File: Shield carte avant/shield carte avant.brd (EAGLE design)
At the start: 68.6 x 53.3 mm, 23 parts, among them IC1 MCP2562-E_P, IC2 MCP2515-I_P, J1 22-05-7078-07, J2 22-05-7028-02, J3 22-05-7038-03, J5 22-05-7028-02, M1 ARDUINO_R3_ICSP

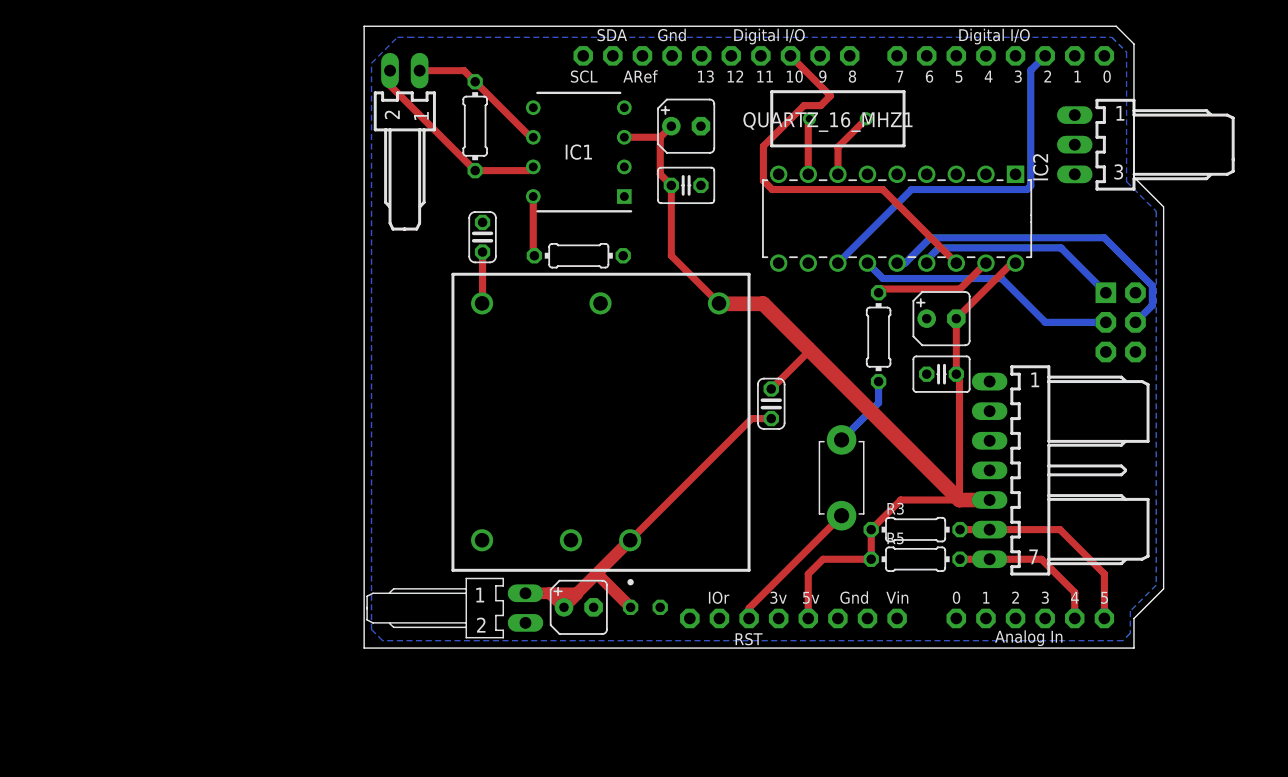
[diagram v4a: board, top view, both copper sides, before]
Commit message: Début ajout relais pour les boutons lumineux
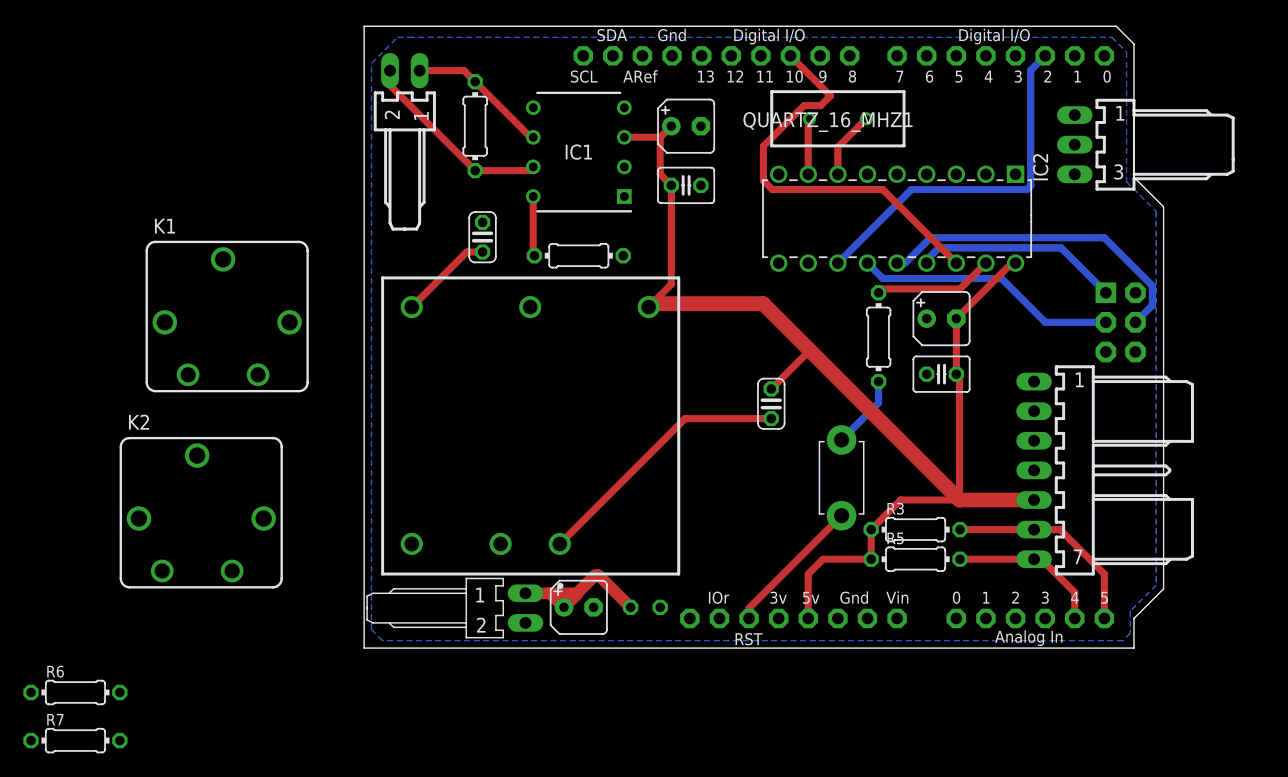
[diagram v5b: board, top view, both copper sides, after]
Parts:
- added K1, K2: CP1-12V, relay:CP1
- added R6, R7: 100R, rcl:0204/7
- moved PS1 6.04 mm to (2.86, 31.8)
- moved J1 3.81 mm to (58.7, 15.2)
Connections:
- new net S$1: C4.2, PS1.1
- net +12V: now also K1.1, K1.C, K2.1, K2.C; no longer C4.2, PS1.1
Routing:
- net S$1: track 0.00 -> 22.6 mm
- net +12V: track 34.9 -> 14.2 mm
- net +5V: track 99.4 -> 108.7 mm
- net N$3: track 4.42 -> 8.03 mm

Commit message: Ajout des MOSFET pour gérer l'affichage des boutons
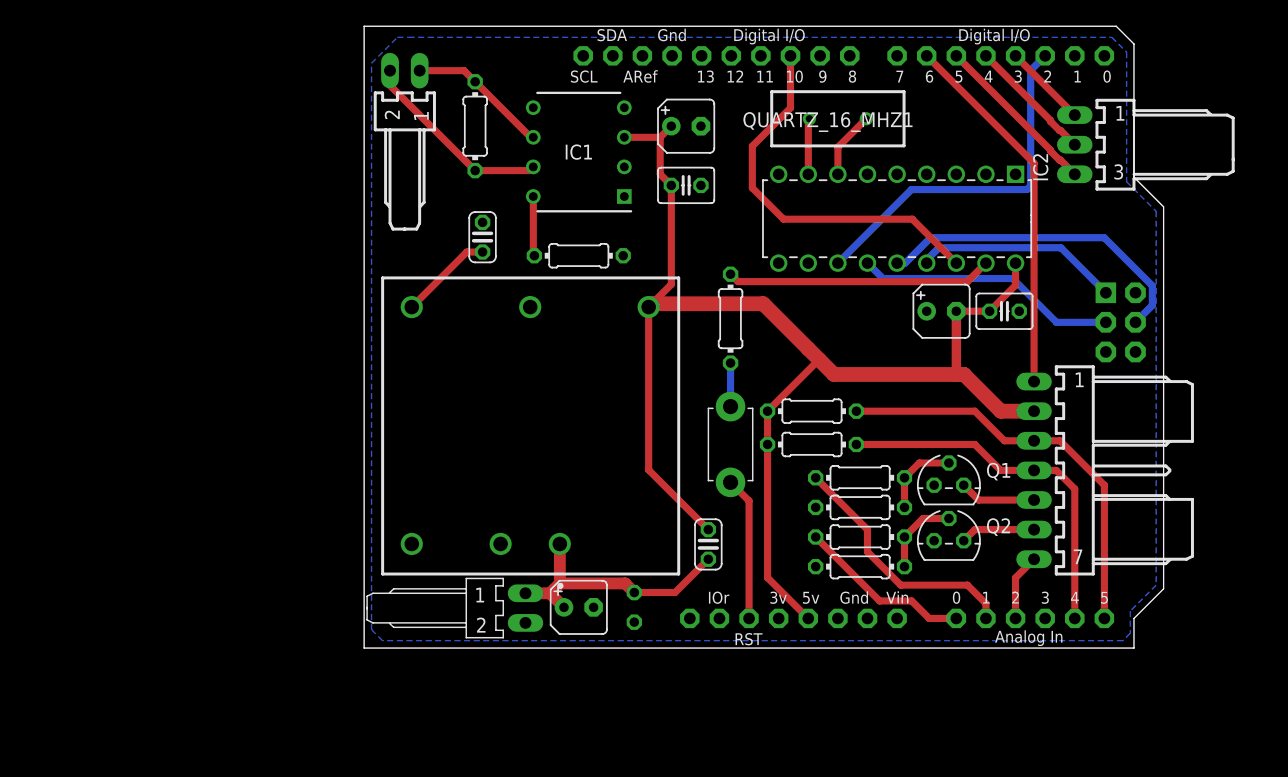
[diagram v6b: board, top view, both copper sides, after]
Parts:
- removed C4: 680 pF, rcl:C025-024X044
- removed K1, K2: CP1-12V, relay:CP1
- added C1: 680 pF, rcl:C025-024X044
- added Q1, Q2: (no value), transistors:TO-92
- added R8, R9: 100, rcl:0204/7
- R6, R7: value 100R -> 10k
- moved R7 70.2 mm to (43.8, 12.1)
- moved R6 68.2 mm to (43.8, 6.99)
- moved R3 13.5 mm to (39.7, 20.3)
- moved R5 13.3 mm to (39.7, 17.5)
- moved R4 12.8 mm to (32.7, 28.3)
- moved SW2 9.94 mm to (32.7, 17.5)
- moved C8 7.63 mm to (56.2, 28.9), turned to 180 degrees
- moved C3 0.95 mm to (24.4, 3.49), turned to 270 degrees
- moved C2 0.63 mm to (50.8, 28.9)
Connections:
- removed net D1: J3.1
- removed net D2: J3.2
- removed net D3: J3.3
- removed net D4: J1.1
- removed net D5: J1.2
- removed net D6: J1.3
- removed net D7: J1.4
- removed net S$1: C4.2, PS1.1
- removed net SCL: J1.6, M1.A5, R3.2
- removed net SDA: J1.7, M1.A4, R5.2
- new net ERROR: J1.6, Q2.3
- new net ERROR_MOTOR: M1.A0, R8.2
- new net HOMMING: M1.D12
- new net LAUNCH: J1.5, Q1.3
- new net LAUNCH_LED: M1.A1, R9.2
- new net LAUNCH_STATE: J1.7, M1.A2
- new net N$12: Q2.2, R6.2, R8.1
- new net N$13: Q1.2, R7.2, R9.1
- new net NEUTRE: J1.1, M1.D6
- new net SCL_I2C: J1.3, M1.A5, R3.2
- new net SCL_SPI: J3.3, M1.D5
- new net SDA_I2C: J1.4, M1.A4, R5.2
- new net SDA_SPI: J3.2, M1.D4
- new net TV: J3.1, M1.D3
- net +12V: now also C1.1, PS1.1; no longer K1.1, K1.C, K2.1, K2.C
- net +5V: now also C1.2, J1.2; no longer C4.1, J1.5
- net GND: now also Q1.1, Q2.1, R6.1, R7.1
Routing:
- net SCL_I2C: track 0.00 -> 35.3 mm
- net NEUTRE: track 0.00 -> 31.8 mm
- net SDA_I2C: track 0.00 -> 31.4 mm
- net S$1: track 22.6 -> 0.00 mm
- net LAUNCH_LED: track 0.00 -> 21.5 mm
- net SCL: track 17.8 -> 0.00 mm
- net ERROR_MOTOR: track 0.00 -> 15.0 mm
- net SCL_SPI: track 0.00 -> 14.4 mm
- net SDA: track 13.2 -> 0.00 mm
- net N$11: track 10.3 -> 22.8 mm
- net SDA_SPI: track 0.00 -> 10.8 mm
- net +5V: track 108.7 -> 117.5 mm
- net +12V: track 14.2 -> 22.6 mm
- net TV: track 0.00 -> 7.18 mm
- net N$12: track 0.00 -> 7.01 mm
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
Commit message: Fin du routage et vérification sérigraphie
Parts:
- moved J2 12.4 mm to (5.08, 37.1), turned to 180 degrees
- moved R2 1.59 mm to (10.8, 43.2)
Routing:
- net N$8: track 12.1 -> 20.3 mm
- net N$5: track 16.7 -> 11.1 mm
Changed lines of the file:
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@@
 <element name="C5" library="rcl" library_urn="urn:adsk.eagle:library:334" package="C025-024X044" package3d_urn="urn:adsk.eagle:package:23630/1" value="680 pF" x="11.43" y="35.2425" smashed="yes" rot="R90">
 <attribute name="SPICEPREFIX" value="C" x="11.43" y="35.2425" size="1.778" layer="27" rot="R90" display="off"/>
-<attribute name="VALUE" x="9.3345" y="33.147" size="1.27" layer="27" ratio="10" rot="R90"/>
-</element>
-<element name="J2" library="con-molex" library_urn="urn:adsk.eagle:library:165" package="7395-02" value="22-05-7028-02" x="4.7625" y="49.53" smashed="yes">
-<attribute name="MF" value="MOLEX" x="4.7625" y="49.53" size="1.778" layer="27" display="off"/>
-<attribute name="MPN" value="" x="4.7625" y="49.53" size="1.778" layer="27" display="off"/>
-<attribute name="OC_FARNELL" value="9731601" x="4.7625" y="49.53" size="1.778" layer="27" display="off"/>
-<attribute name="OC_NEWARK" value="unknown" x="4.7625" y="49.53" size="1.778" layer="27" display="off"/>
-</element>
-<element name="R2" library="rcl" library_urn="urn:adsk.eagle:library:334" package="0204/7" package3d_urn="urn:adsk.eagle:package:23498/1" value="120 " x="10.795" y="44.7675" smashed="yes" rot="R90">
-<attribute name="SPICEPREFIX" value="R" x="10.795" y="44.7675" size="1.778" layer="27" rot="R90" display="off"/>
-<attribute name="VALUE" x="10.3124" y="46.3931" size="0.9906" layer="27" ratio="10" rot="R270"/>
+<attribute name="VALUE" x="9.652" y="33.147" size="1.27" layer="27" ratio="10" rot="R90"/>
+</element>
+<element name="J2" library="con-molex" library_urn="urn:adsk.eagle:library:165" package="7395-02" value="22-05-7028-02" x="5.08" y="37.1475" smashed="yes" rot="R180">
+<attribute name="MF" value="MOLEX" x="5.08" y="37.1475" size="1.778" layer="27" rot="R180" display="off"/>
+<attribute name="MPN" value="" x="5.08" y="37.1475" size="1.778" layer="27" rot="R180" display="off"/>
+<attribute name="OC_FARNELL" value="9731601" x="5.08" y="37.1475" size="1.778" layer="27" rot="R180" display="off"/>
+<attribute name="OC_NEWARK" value="unknown" x="5.08" y="37.1475" size="1.778" layer="27" rot="R180" display="off"/>
+</element>
+<element name="R2" library="rcl" library_urn="urn:adsk.eagle:library:334" package="0204/7" package3d_urn="urn:adsk.eagle:package:23498/1" value="120 " x="10.795" y="43.18" smashed="yes" rot="R90">
+<attribute name="SPICEPREFIX" value="R" x="10.795" y="43.18" size="1.778" layer="27" rot="R90" display="off"/>
+<attribute name="VALUE" x="10.3124" y="44.8056" size="0.9906" layer="27" ratio="10" rot="R270"/>
 </element>
 <element name="M1" library="adafruit" package="ARDUINOR3_ICSP" value="ARDUINO_R3_ICSP" x="1.27" y="0" smashed="yes"/>
@@
 <element name="C9" library="rcl" library_urn="urn:adsk.eagle:library:334" package="B45181A" package3d_urn="urn:adsk.eagle:package:23316/1" value="1µF" x="28.8925" y="44.7675" smashed="yes">
 <attribute name="SPICEPREFIX" value="C" x="28.8925" y="44.7675" size="1.778" layer="27" display="off"/>
-<attribute name="VALUE" x="31.9405" y="43.1165" size="1.27" layer="27" ratio="10"/>
+<attribute name="VALUE" x="31.623" y="43.7515" size="1.27" layer="27" ratio="10"/>
 </element>
 <element name="C10" library="rcl" library_urn="urn:adsk.eagle:library:334" package="C025-030X050" package3d_urn="urn:adsk.eagle:package:23631/1" value="27pF" x="28.8925" y="39.6875" smashed="yes">
@@
 <attribute name="MANUFACTURER_NAME" value="Fox" x="41.91" y="45.4025" size="1.778" layer="27" display="off"/>
 <attribute name="MANUFACTURER_PART_NUMBER" value="FOXSLF/160-20" x="41.91" y="45.4025" size="1.778" layer="27" display="off"/>
-<attribute name="NAME" x="41.087" y="45.3205" size="1.27" layer="25" align="center"/>
+<attribute name="NAME" x="42.0395" y="46.5905" size="0.8128" layer="25" align="center"/>
 <attribute name="RS_PART_NUMBER" value="1734298" x="41.91" y="45.4025" size="1.778" layer="27" display="off"/>
 </element>
@@
 <element name="C1" library="rcl" library_urn="urn:adsk.eagle:library:334" package="C025-024X044" package3d_urn="urn:adsk.eagle:package:23630/1" value="680 pF" x="30.7975" y="8.89" smashed="yes" rot="R90">
 <attribute name="SPICEPREFIX" value="C" x="30.7975" y="8.89" size="1.778" layer="27" rot="R90" display="off"/>
-<attribute name="VALUE" x="33.4645" y="7.112" size="1.27" layer="27" ratio="10" rot="R90"/>
+<attribute name="VALUE" x="33.4645" y="6.477" size="1.27" layer="27" ratio="10" rot="R90"/>
 </element>
 <element name="Q1" library="transistors" package="TO-92" value="" x="51.435" y="13.97" smashed="yes">
-<attribute name="NAME" x="54.61" y="14.605" size="1.27" layer="25" ratio="10"/>
 <attribute name="VALUE" x="54.61" y="12.7" size="1.27" layer="27" ratio="10"/>
 </element>
 <element name="Q2" library="transistors" package="TO-92" value="" x="51.435" y="9.2075" smashed="yes">
-<attribute name="NAME" x="54.61" y="9.8425" size="1.27" layer="25" ratio="10"/>
 <attribute name="VALUE" x="54.61" y="7.9375" size="1.27" layer="27" ratio="10"/>
 </element>
@@
 <contactref element="IC1" pad="7"/>
 <contactref element="J2" pad="2"/>
-<wire x1="3.4925" y1="49.53" x2="3.4925" y2="48.26" width="0.6096" layer="1"/>
-<wire x1="3.4925" y1="48.26" x2="10.795" y2="40.9575" width="0.6096" layer="1"/>
-<wire x1="10.795" y1="40.9575" x2="15.4625" y2="40.9575" width="0.6096" layer="1"/>
-<wire x1="15.4625" y1="40.9575" x2="15.78" y2="41.275" width="0.6096" layer="1"/>
+<wire x1="10.795" y1="39.37" x2="13.875" y2="39.37" width="0.6096" layer="1"/>
+<wire x1="13.875" y1="39.37" x2="15.78" y2="41.275" width="0.6096" layer="1"/>
+<wire x1="10.795" y1="39.37" x2="8.5725" y2="39.37" width="0.6096" layer="1"/>
+<wire x1="8.5725" y1="39.37" x2="6.35" y2="37.1475" width="0.6096" layer="1"/>
 </signal>
 <signal name="N$8">
@@
 <contactref element="IC1" pad="6"/>
 <contactref element="J2" pad="1"/>
-<wire x1="6.0325" y1="49.53" x2="9.8425" y2="49.53" width="0.6096" layer="1"/>
-<wire x1="9.8425" y1="49.53" x2="10.795" y2="48.5775" width="0.6096" layer="1"/>
-<wire x1="10.795" y1="48.5775" x2="15.5575" y2="43.815" width="0.6096" layer="1"/>
-<wire x1="15.5575" y1="43.815" x2="15.78" y2="43.815" width="0.6096" layer="1"/>
+<wire x1="14.9225" y1="43.815" x2="11.7475" y2="46.99" width="0.6096" layer="1"/>
+<wire x1="10.795" y1="46.99" x2="11.7475" y2="46.99" width="0.6096" layer="1"/>
+<wire x1="14.9225" y1="43.815" x2="15.78" y2="43.815" width="0.6096" layer="1"/>
+<wire x1="10.795" y1="46.99" x2="8.5725" y2="46.99" width="0.6096" layer="1"/>
+<wire x1="8.5725" y1="46.99" x2="3.81" y2="42.2275" width="0.6096" layer="1"/>
+<wire x1="3.81" y1="42.2275" x2="3.81" y2="37.1475" width="0.6096" layer="1"/>
 </signal>
 <signal name="LAUNCH">

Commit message: Sérigraphie
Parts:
- C3: value 4.7 uF -> 27 pF
- C6: value (none) -> 1 µF
- moved R3 4.14 mm to (43.8, 20.0)
- moved R5 4.13 mm to (43.8, 17.5)
- moved R4 0.71 mm to (32.4, 27.6)
- flipped C3 to the top
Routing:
- net SCL_I2C: track 35.3 -> 31.1 mm
- net SDA_I2C: track 31.4 -> 27.3 mm
- net +5V: track 117.5 -> 114.9 mm
- net N$2: track 3.74 -> 3.23 mm
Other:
- board text added: "CAN"
- board text added: "Dash 2"
- board text added: "Dashboard 1"
- board text added: "Dashboard controller OPTIMUS v1.0"
- board text added: "Power"
